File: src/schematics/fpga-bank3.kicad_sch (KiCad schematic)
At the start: 5 parts, among them U6 LFE5U-85F-*BG756*

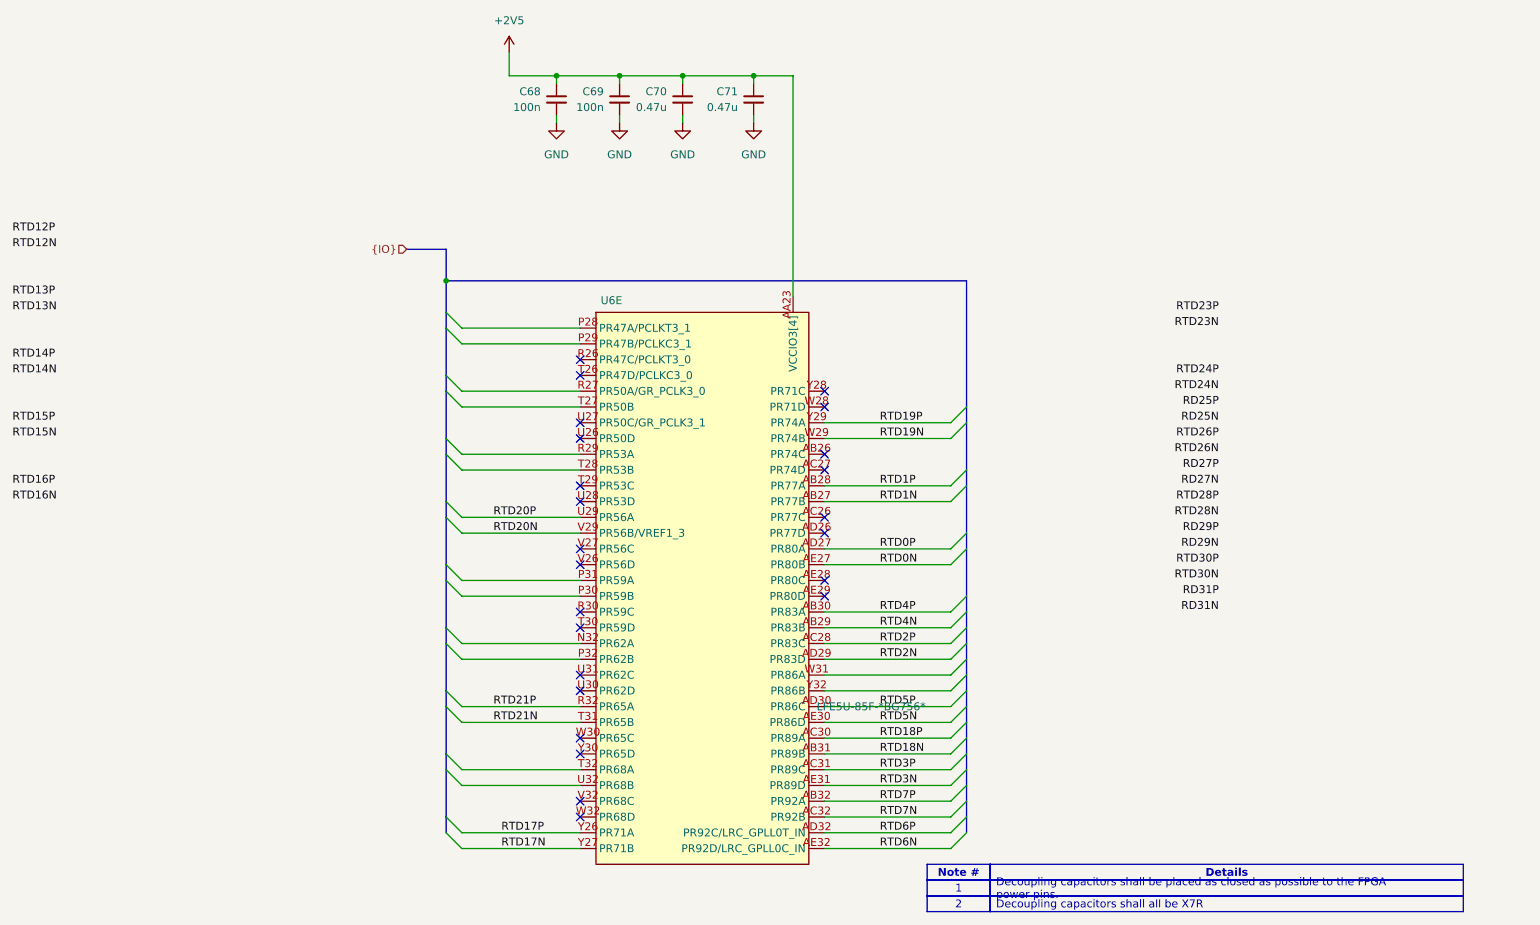
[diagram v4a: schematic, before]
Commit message: Finish routing the io connector
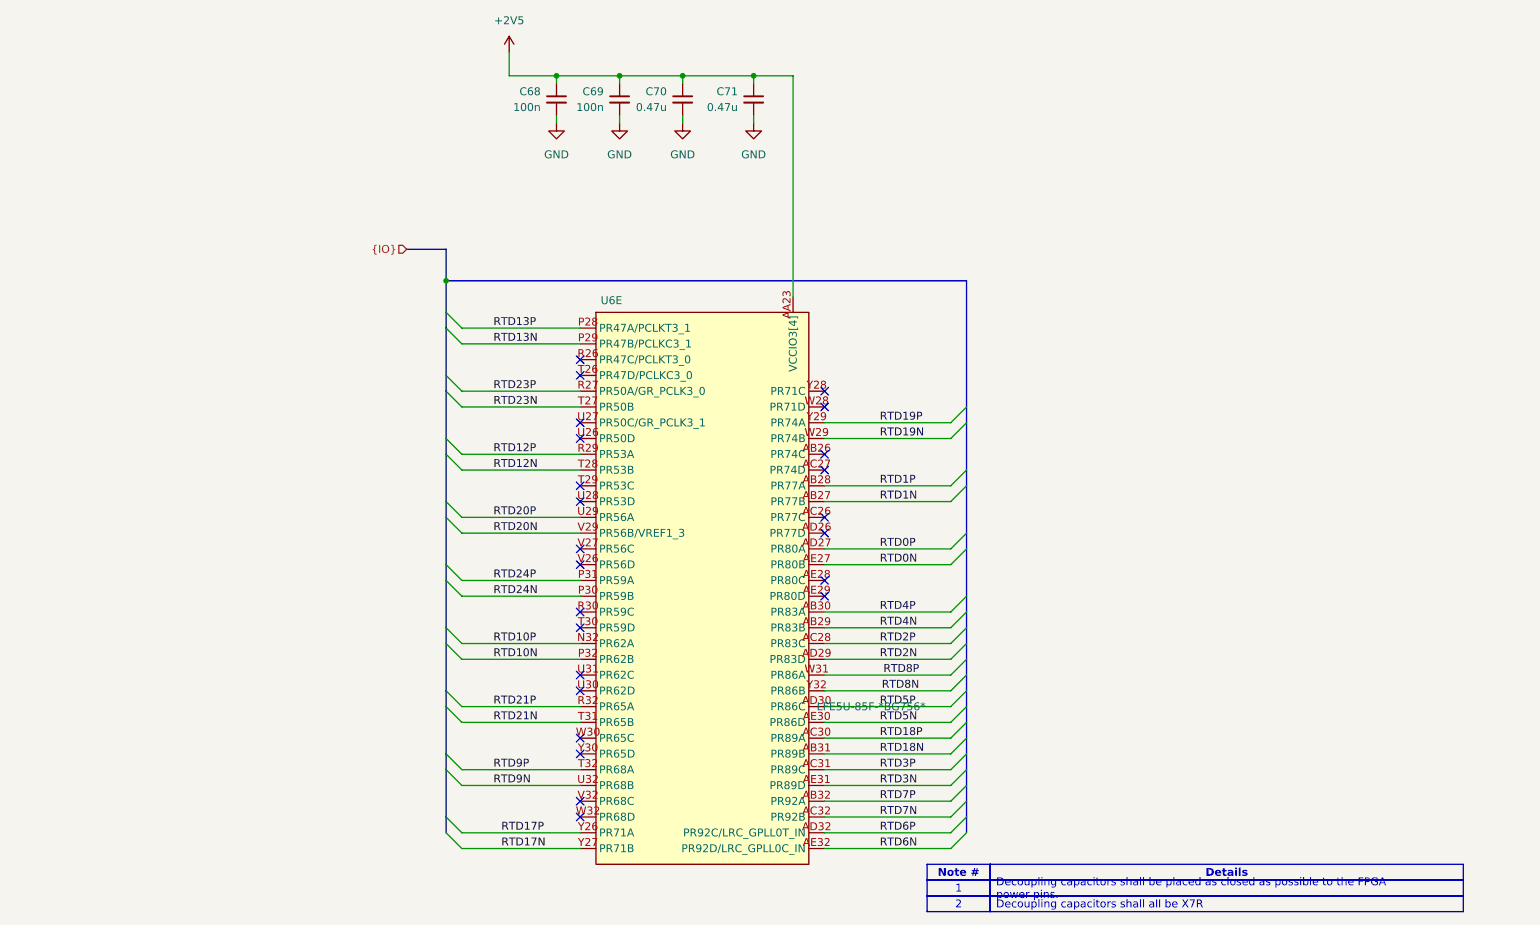
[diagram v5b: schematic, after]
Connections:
- net RTD12N: now also U6.T28 (PR53B)
- net RTD12P: now also U6.R29 (PR53A)
- net RTD13N: now also U6.P29 (PR47B/PCLKC3_1)
- net RTD13P: now also U6.P28 (PR47A/PCLKT3_1)
- net RTD23N: now also U6.T27 (PR50B)
- net RTD23P: now also U6.R27 (PR50A/GR_PCLK3_0)
- net RTD24N: now also U6.P30 (PR59B)
- net RTD24P: now also U6.P31 (PR59A)
- net RTD10P: now reaches U6.N32 (PR62A)
- net RTD10N: now reaches U6.P32 (PR62B)
- net RTD9P: now reaches U6.T32 (PR68A)
- net RTD9N: now reaches U6.U32 (PR68B)
- net RTD8P: now reaches U6.W31 (PR86A)
- net RTD8N: now reaches U6.Y32 (PR86B)
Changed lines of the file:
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@@
-		)
-	)
-	(label "RTD12N"
-		(at 45.72 63.5 0)
-		(effects
-			(font
-				(size 1.27 1.27)
-			)
-			(justify left bottom)
-		)
-	)
-	(label "RTD13N"
-		(at 45.72 73.66 0)
-		(effects
-			(font
-				(size 1.27 1.27)
-			)
-			(justify left bottom)
 		)
 	)
@@
 	)
 	(label "RTD24P"
-		(at 240.03 83.82 180)
-		(effects
-			(font
-				(size 1.27 1.27)
-			)
-			(justify right bottom)
+		(at 123.19 116.84 0)
+		(effects
+			(font
+				(size 1.27 1.27)
+			)
+			(justify left bottom)
+		)
+	)
+	(label "RTD13P"
+		(at 123.19 76.2 0)
+		(effects
+			(font
+				(size 1.27 1.27)
+			)
+			(justify left bottom)
 		)
 	)
@@
 		)
 	)
+	(label "RTD9N"
+		(at 123.19 149.86 0)
+		(effects
+			(font
+				(size 1.27 1.27)
+			)
+			(justify left bottom)
+		)
+	)
 	(label "RTD18P"
 		(at 185.42 142.24 0)
@@
 		)
 	)
-	(label "RD29P"
-		(at 240.03 109.22 180)
-		(effects
-			(font
-				(size 1.27 1.27)
-			)
-			(justify right bottom)
-		)
-	)
 	(label "RTD20P"
 		(at 123.19 106.68 0)
@@
 		)
 	)
-	(label "RD31P"
-		(at 240.03 119.38 180)
-		(effects
-			(font
-				(size 1.27 1.27)
-			)
-			(justify right bottom)
-		)
-	)
 	(label "RTD17P"
 		(at 124.46 157.48 0)
@@
 		)
 	)
+	(label "RTD12P"
+		(at 123.19 96.52 0)
+		(effects
+			(font
+				(size 1.27 1.27)
+			)
+			(justify left bottom)
+		)
+	)
 	(label "RTD5N"
 		(at 185.42 139.7 0)
@@
 		)
 	)
-	(label "RTD30P"
-		(at 240.03 114.3 180)
-		(effects
-			(font
-				(size 1.27 1.27)
-			)
-			(justify right bottom)
-		)
-	)
 	(label "RTD7P"
 		(at 185.42 152.4 0)
@@
 		)
 	)
-	(label "RD31N"
-		(at 240.03 121.92 180)
-		(effects
-			(font
-				(size 1.27 1.27)
-			)
-			(justify right bottom)
-		)
-	)
 	(label "RTD0P"
 		(at 185.42 111.76 0)
@@
 		)
 	)
-	(label "RTD26P"
-		(at 240.03 93.98 180)
-		(effects
-			(font
-				(size 1.27 1.27)
-			)
-			(justify right bottom)
-		)
-	)
-	(label "RTD13P"
-		(at 45.72 71.12 0)
-		(effects
-			(font
-				(size 1.27 1.27)
-			)
-			(justify left bottom)
-		)
-	)
 	(label "RTD1P"
 		(at 185.42 101.6 0)
@@
 		)
 	)
-	(label "RTD26N"
-		(at 240.03 96.52 180)
-		(effects
-			(font
-				(size 1.27 1.27)
-			)
-			(justify right bottom)
-		)
-	)
-	(label "RD25P"
-		(at 240.03 88.9 180)
-		(effects
-			(font
-				(size 1.27 1.27)
-			)
-			(justify right bottom)
+	(label "RTD10P"
+		(at 123.19 127 0)
+		(effects
+			(font
+				(size 1.27 1.27)
+			)
+			(justify left bottom)
 		)
 	)
@@
 	)
 	(label "RTD24N"
-		(at 240.03 86.36 180)
-		(effects
-			(font
-				(size 1.27 1.27)
-			)
-			(justify right bottom)
+		(at 123.19 119.38 0)
+		(effects
+			(font
+				(size 1.27 1.27)
+			)
+			(justify left bottom)
+		)
+	)
+	(label "RTD12N"
+		(at 123.19 99.06 0)
+		(effects
+			(font
+				(size 1.27 1.27)
+			)
+			(justify left bottom)
 		)
 	)
 	(label "RTD23P"
-		(at 240.03 73.66 180)
-		(effects
-			(font
-				(size 1.27 1.27)
-			)
-			(justify right bottom)
-		)
-	)
-	(label "RTD30N"
-		(at 240.03 116.84 180)
-		(effects
-			(font
-				(size 1.27 1.27)
-			)
-			(justify right bottom)
+		(at 123.19 86.36 0)
+		(effects
+			(font
+				(size 1.27 1.27)
+			)
+			(justify left bottom)
+		)
+	)
+	(label "RTD13N"
+		(at 123.19 78.74 0)
+		(effects
+			(font
+				(size 1.27 1.27)
+			)
+			(justify left bottom)
 		)
 	)
@@
 		)
 	)
-	(label "RTD12P"
-		(at 45.72 60.96 0)
-		(effects
-			(font
-				(size 1.27 1.27)
-			)
-			(justify left bottom)
-		)
-	)
 	(label "RTD17N"
 		(at 124.46 160.02 0)
@@
 		)
 	)
-	(label "RTD28N"
-		(at 240.03 106.68 180)
-		(effects
-			(font
-				(size 1.27 1.27)
-			)
-			(justify right bottom)
-		)
-	)
-	(label "RTD16N"
-		(at 45.72 104.14 0)
-		(effects
-			(font
-				(size 1.27 1.27)
-			)
-			(justify left bottom)
-		)
-	)
 	(label "RTD6P"
 		(at 185.42 157.48 0)
@@
 		)
 	)
-	(label "RTD14N"
-		(at 45.72 83.82 0)
-		(effects
-			(font
-				(size 1.27 1.27)
-			)
-			(justify left bottom)
-		)
-	)
-	(label "RTD16P"
-		(at 45.72 101.6 0)
-		(effects
-			(font
-				(size 1.27 1.27)
-			)
-			(justify left bottom)
-		)
-	)
-	(label "RD25N"
-		(at 240.03 91.44 180)
+	(label "RTD8N"
+		(at 191.77 134.62 180)
 		(effects
 			(font
@@
 		)
 	)
-	(label "RTD28P"
-		(at 240.03 104.14 180)
+	(label "RTD8P"
+		(at 191.77 132.08 180)
 		(effects
 			(font
@@
 			)
 			(justify right bottom)
+		)
+	)
+	(label "RTD10N"
+		(at 123.19 129.54 0)
+		(effects
+			(font
+				(size 1.27 1.27)
+			)
+			(justify left bottom)
+		)
+	)
+	(label "RTD9P"
+		(at 123.19 147.32 0)
+		(effects
+			(font
+				(size 1.27 1.27)
+			)
+			(justify left bottom)
 		)
 	)
@@
 		)
 	)
-	(label "RD27N"
-		(at 240.03 101.6 180)
-		(effects
-			(font
-				(size 1.27 1.27)
-			)
-			(justify right bottom)
-		)
-	)
 	(label "RTD19P"
 		(at 185.42 91.44 0)
@@
 		)
 	)
-	(label "RTD15P"
-		(at 45.72 91.44 0)
-		(effects
-			(font
-				(size 1.27 1.27)
-			)
-			(justify left bottom)
-		)
-	)
-	(label "RD27P"
-		(at 240.03 99.06 180)
-		(effects
-			(font
-				(size 1.27 1.27)
-			)
-			(justify right bottom)
-		)
-	)
-	(label "RTD15N"
-		(at 45.72 93.98 0)
-		(effects
-			(font
-				(size 1.27 1.27)
-			)
-			(justify left bottom)
-		)
-	)
 	(label "RTD2P"
 		(at 185.42 127 0)
@@
 	)
 	(label "RTD23N"
-		(at 240.03 76.2 180)
-		(effects
-			(font
-				(size 1.27 1.27)
-			)
-			(justify right bottom)
-		)
-	)
-	(label "RTD14P"
-		(at 45.72 81.28 0)
-		(effects
-			(font
-				(size 1.27 1.27)
-			)
-			(justify left bottom)
-		)
-	)
-	(label "RD29N"
-		(at 240.03 111.76 180)
-		(effects
-			(font
-				(size 1.27 1.27)
-			)
-			(justify right bottom)
-		)
-	)
+		(at 123.19 88.9 0)
+		(effects
+			(font
+				(size 1.27 1.27)
+			)
+			(justify left bottom)
+		)
+	)

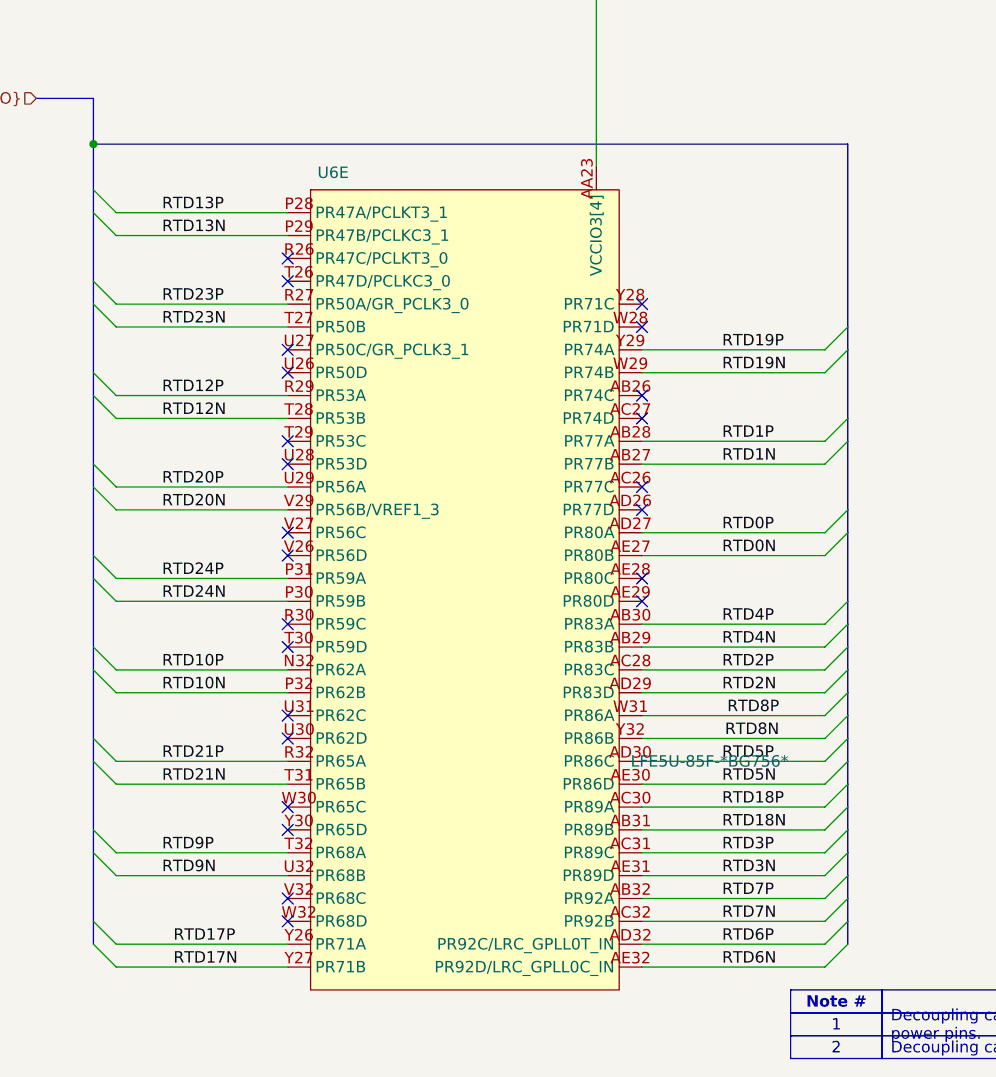
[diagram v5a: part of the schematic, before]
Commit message: Fix diff pair skew
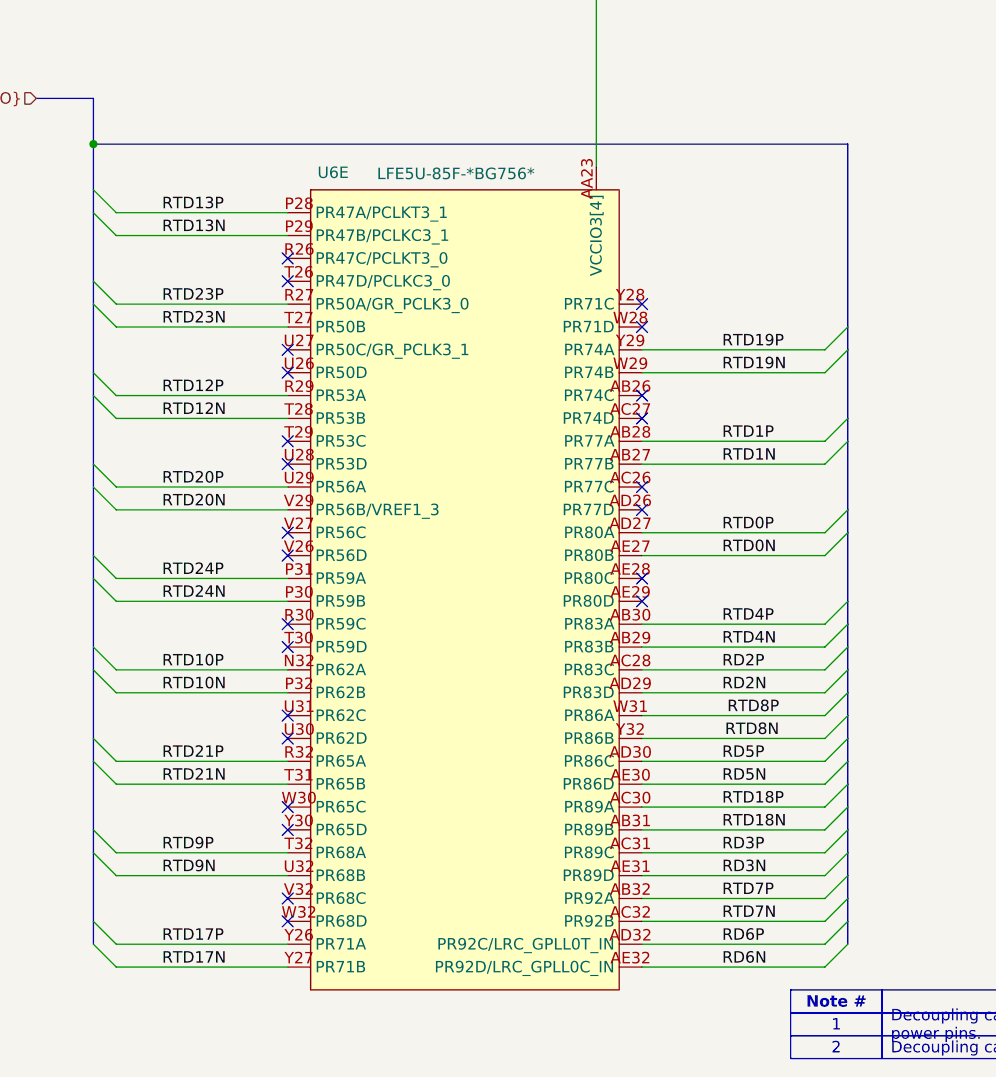
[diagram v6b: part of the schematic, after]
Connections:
- net RTD2N renamed RD2N
- net RTD2P renamed RD2P
- net RTD3N renamed RD3N
- net RTD3P renamed RD3P
- net RTD5N renamed RD5N
- net RTD5P renamed RD5P
- net RTD6N renamed RD6N
- net RTD6P renamed RD6P
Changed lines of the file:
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@@
 		)
 	)
-	(label "RTD2N"
+	(label "RD2N"
 		(at 185.42 129.54 0)
 		(effects
@@
 		)
 	)
-	(label "RTD3N"
+	(label "RD3N"
 		(at 185.42 149.86 0)
 		(effects
@@
 	)
 	(label "RTD17P"
-		(at 124.46 157.48 0)
+		(at 123.19 157.48 0)
 		(effects
 			(font
@@
 		)
 	)
-	(label "RTD5N"
+	(label "RD5N"
 		(at 185.42 139.7 0)
 		(effects
@@
 		)
 	)
-	(label "RTD3P"
+	(label "RD3P"
 		(at 185.42 147.32 0)
 		(effects
@@
 		)
 	)
-	(label "RTD6N"
+	(label "RD6N"
 		(at 185.42 160.02 0)
 		(effects
@@
 	)
 	(label "RTD17N"
-		(at 124.46 160.02 0)
-		(effects
-			(font
-				(size 1.27 1.27)
-			)
-			(justify left bottom)
-		)
-	)
-	(label "RTD6P"
+		(at 123.19 160.02 0)
+		(effects
+			(font
+				(size 1.27 1.27)
+			)
+			(justify left bottom)
+		)
+	)
+	(label "RD6P"
 		(at 185.42 157.48 0)
 		(effects
@@
 		)
 	)
-	(label "RTD5P"
+	(label "RD5P"
 		(at 185.42 137.16 0)
 		(effects
@@
 		)
 	)
-	(label "RTD2P"
+	(label "RD2P"
 		(at 185.42 127 0)
 		(effects
@@
 		)
 		(property "Value" "LFE5U-85F-*BG756*"
-			(at 175.26 137.16 0)
-			(effects
-				(font
+			(at 147.066 71.882 0)
+			(effects
+				(font

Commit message: Add bom components
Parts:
- C68, C69: MPN (none) -> GRM033R60J104ME19J; Manufacturer (none) -> Murata Electronics; Mouting Technology (none) -> SMD
- C70, C71: value 0.47u -> 470n; MPN (none) -> GRM033R60J474KE90J; Manufacturer (none) -> Murata Electronics; Mouting Technology (none) -> SMD
- U6: MPN (none) -> LFE5U-85F-6BG756C; Manufacturer (none) -> Lattice; Mouting Technology (none) -> SMD
